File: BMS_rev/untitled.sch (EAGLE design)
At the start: 26 parts, among them J1 U.FL-R-SMT(01), U1 ESP32-DEVKITC-32D, U2 PCF8574AT

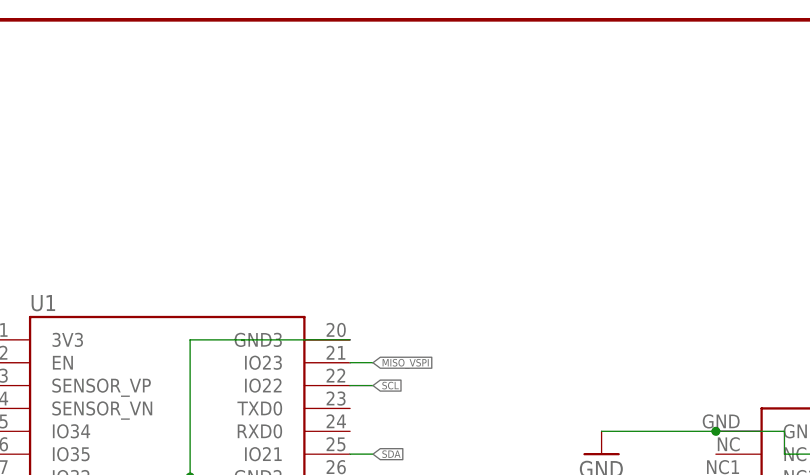
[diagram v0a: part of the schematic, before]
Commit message: menambahkan pullup i2c
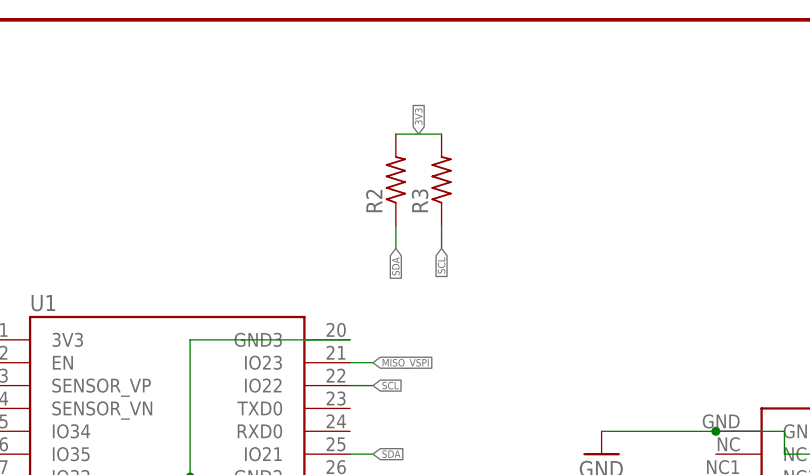
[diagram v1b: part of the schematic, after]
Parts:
- added R2, R3: (no value), adafruit:R-US_M0805
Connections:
- net 3V3: now also R2.2, R3.2
- net SCL: now also R3.1
- net SDA: now also R2.1
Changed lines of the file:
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@@
 <part name="CONN2P-3.5PI5" library="CONN2P-3.5PI" deviceset="CONN2P-3.5PI" device=""/>
 <part name="R1" library="adafruit" library_urn="urn:adsk.eagle:library:420" deviceset="R-US_" device="M0805" package3d_urn="urn:adsk.eagle:package:6240587/1"/>
+<part name="R2" library="adafruit" library_urn="urn:adsk.eagle:library:420" deviceset="R-US_" device="M0805" package3d_urn="urn:adsk.eagle:package:6240587/1"/>
+<part name="R3" library="adafruit" library_urn="urn:adsk.eagle:library:420" deviceset="R-US_" device="M0805" package3d_urn="urn:adsk.eagle:package:6240587/1"/>
 </parts>
 <sheets>
@@
 <attribute name="NAME" x="-42.1386" y="-82.55" size="1.778" layer="95" rot="R90"/>
 <attribute name="VALUE" x="-37.338" y="-82.55" size="1.778" layer="96" rot="R90"/>
+</instance>
+<instance part="R2" gate="G$1" x="-40.64" y="177.8" smashed="yes" rot="R90">
+<attribute name="NAME" x="-42.1386" y="173.99" size="1.778" layer="95" rot="R90"/>
+<attribute name="VALUE" x="-37.338" y="173.99" size="1.778" layer="96" rot="R90"/>
+</instance>
+<instance part="R3" gate="G$1" x="-35.56" y="177.8" smashed="yes" rot="R90">
+<attribute name="NAME" x="-37.0586" y="173.99" size="1.778" layer="95" rot="R90"/>
+<attribute name="VALUE" x="-32.258" y="173.99" size="1.778" layer="96" rot="R90"/>
 </instance>
 </instances>
@@
 <label x="-40.64" y="-71.12" size="0.8128" layer="95" rot="R90" xref="yes"/>
 </segment>
+<segment>
+<pinref part="R2" gate="G$1" pin="2"/>
+<pinref part="R3" gate="G$1" pin="2"/>
+<wire x1="-40.64" y1="182.88" x2="-35.56" y2="182.88" width="0.1524" layer="91"/>
+<label x="-38.1" y="182.88" size="0.8128" layer="95" rot="R90" xref="yes"/>
+</segment>
 </net>
 <net name="LORA_DI1" class="0">
@@
 <label x="-33.02" y="-83.82" size="0.8128" layer="95" rot="R90" xref="yes"/>
 </segment>
+<segment>
+<pinref part="R3" gate="G$1" pin="1"/>
+<wire x1="-35.56" y1="172.72" x2="-35.56" y2="170.18" width="0.1524" layer="91"/>
+<label x="-35.56" y="170.18" size="0.8128" layer="95" rot="R270" xref="yes"/>
+</segment>
 </net>
 <net name="SDA" class="0">
@@
 <label x="-30.48" y="-83.82" size="0.8128" layer="95" rot="R90" xref="yes"/>
 </segment>
-</net>
+<segment>
+<pinref part="R2" gate="G$1" pin="1"/>
+<wire x1="-40.64" y1="172.72" x2="-40.64" y2="170.18" width="0.1524" layer="91"/>
+<label x="-40.64" y="170.18" size="0.8128" layer="95" rot="R270" xref="yes"/>
+</segment>
+</net>

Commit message: PCB BMS
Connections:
- removed net VCC: R28.2, R29.1, U2.VDD
- net OUT+: now also R28.2, R29.1, U2.VDD
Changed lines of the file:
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@@
 <part name="R28" library="rcl" library_urn="urn:adsk.eagle:library:334" deviceset="R-EU_" device="R0805" package3d_urn="urn:adsk.eagle:package:23553/2"/>
 <part name="R29" library="rcl" library_urn="urn:adsk.eagle:library:334" deviceset="R-EU_" device="R0805" package3d_urn="urn:adsk.eagle:package:23553/2"/>
-<part name="P+1" library="supply1" library_urn="urn:adsk.eagle:library:371" deviceset="VCC" device=""/>
 <part name="GND1" library="supply1" library_urn="urn:adsk.eagle:library:371" deviceset="GND" device=""/>
 <part name="J1" library="U.FL-R-SMT_01_" deviceset="U.FL-R-SMT(01)" device=""/>
@@
 <attribute name="VALUE" x="62.23" y="94.742" size="1.778" layer="96" rot="R180"/>
 </instance>
-<instance part="P+1" gate="VCC" x="12.7" y="96.52" smashed="yes">
-<attribute name="VALUE" x="10.16" y="93.98" size="1.778" layer="96" rot="R90"/>
-</instance>
 <instance part="GND1" gate="1" x="12.7" y="68.58" smashed="yes">
 <attribute name="VALUE" x="10.16" y="66.04" size="1.778" layer="96"/>
@@
 <pinref part="R25" gate="G$1" pin="1"/>
 <wire x1="12.7" y1="86.36" x2="15.24" y2="86.36" width="0.1524" layer="91"/>
-</segment>
-</net>
-<net name="VCC" class="0">
-<segment>
-<pinref part="U2" gate="A" pin="VDD"/>
-<pinref part="P+1" gate="VCC" pin="VCC"/>
-<wire x1="15.24" y1="91.44" x2="12.7" y2="91.44" width="0.1524" layer="91"/>
-<wire x1="12.7" y1="91.44" x2="12.7" y2="93.98" width="0.1524" layer="91"/>
-<pinref part="R28" gate="G$1" pin="2"/>
-<wire x1="2.54" y1="76.2" x2="0" y2="76.2" width="0.1524" layer="91"/>
-<wire x1="0" y1="76.2" x2="0" y2="78.74" width="0.1524" layer="91"/>
-<wire x1="0" y1="78.74" x2="35.56" y2="78.74" width="0.1524" layer="91"/>
-<wire x1="35.56" y1="78.74" x2="35.56" y2="91.44" width="0.1524" layer="91"/>
-<pinref part="R29" gate="G$1" pin="1"/>
-<wire x1="63.5" y1="91.44" x2="66.04" y2="91.44" width="0.1524" layer="91"/>
-<wire x1="35.56" y1="93.98" x2="66.04" y2="93.98" width="0.1524" layer="91"/>
-<wire x1="66.04" y1="93.98" x2="66.04" y2="91.44" width="0.1524" layer="91"/>
-<wire x1="35.56" y1="93.98" x2="35.56" y2="91.44" width="0.1524" layer="91"/>
-<wire x1="35.56" y1="91.44" x2="15.24" y2="91.44" width="0.1524" layer="91"/>
-<junction x="15.24" y="91.44"/>
 </segment>
 </net>
@@
 <label x="99.06" y="139.7" size="0.8128" layer="95" xref="yes"/>
 </segment>
-</net>
+<segment>
+<pinref part="U2" gate="A" pin="VDD"/>
+<wire x1="15.24" y1="91.44" x2="12.7" y2="91.44" width="0.1524" layer="91"/>
+<pinref part="R28" gate="G$1" pin="2"/>
+<wire x1="2.54" y1="76.2" x2="0" y2="76.2" width="0.1524" layer="91"/>
+<wire x1="0" y1="76.2" x2="0" y2="78.74" width="0.1524" layer="91"/>
+<wire x1="0" y1="78.74" x2="35.56" y2="78.74" width="0.1524" layer="91"/>
+<wire x1="35.56" y1="78.74" x2="35.56" y2="91.44" width="0.1524" layer="91"/>
+<pinref part="R29" gate="G$1" pin="1"/>
+<wire x1="63.5" y1="91.44" x2="66.04" y2="91.44" width="0.1524" layer="91"/>
+<wire x1="35.56" y1="93.98" x2="66.04" y2="93.98" width="0.1524" layer="91"/>
+<wire x1="66.04" y1="93.98" x2="66.04" y2="91.44" width="0.1524" layer="91"/>
+<wire x1="35.56" y1="93.98" x2="35.56" y2="91.44" width="0.1524" layer="91"/>
+<wire x1="35.56" y1="91.44" x2="15.24" y2="91.44" width="0.1524" layer="91"/>
+<junction x="15.24" y="91.44"/>
+<label x="12.7" y="91.44" size="0.8128" layer="95" rot="R180" xref="yes"/>
+</segment>
+</net>
